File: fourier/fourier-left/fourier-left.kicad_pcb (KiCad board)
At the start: 2 copper layers, 124.4 x 80.4 mm, 129 parts, among them J1 VCC, J3 RGB, J6 C6, J7 GND, U1 ProMicro, U2 TRRS

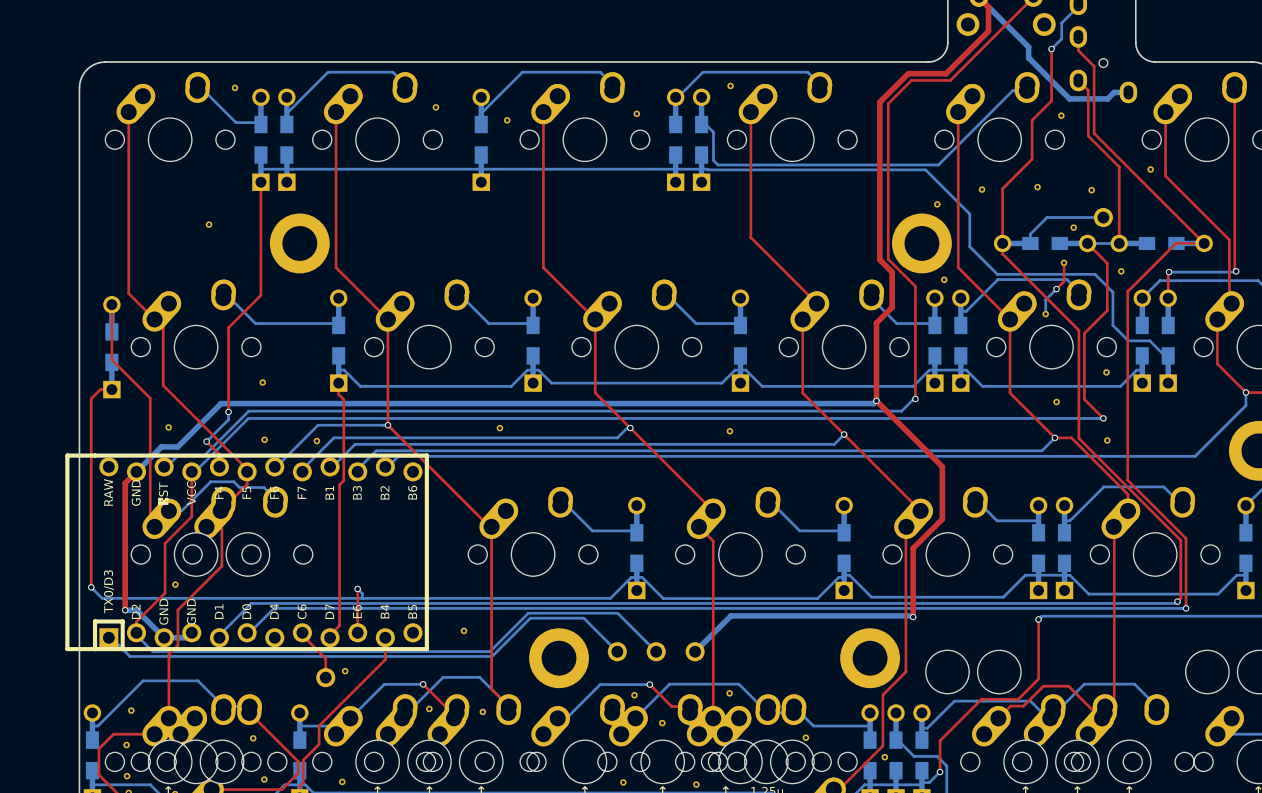
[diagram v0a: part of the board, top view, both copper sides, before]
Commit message: Alas v1
moved pro micro location and added a USB C port for pigtail cables
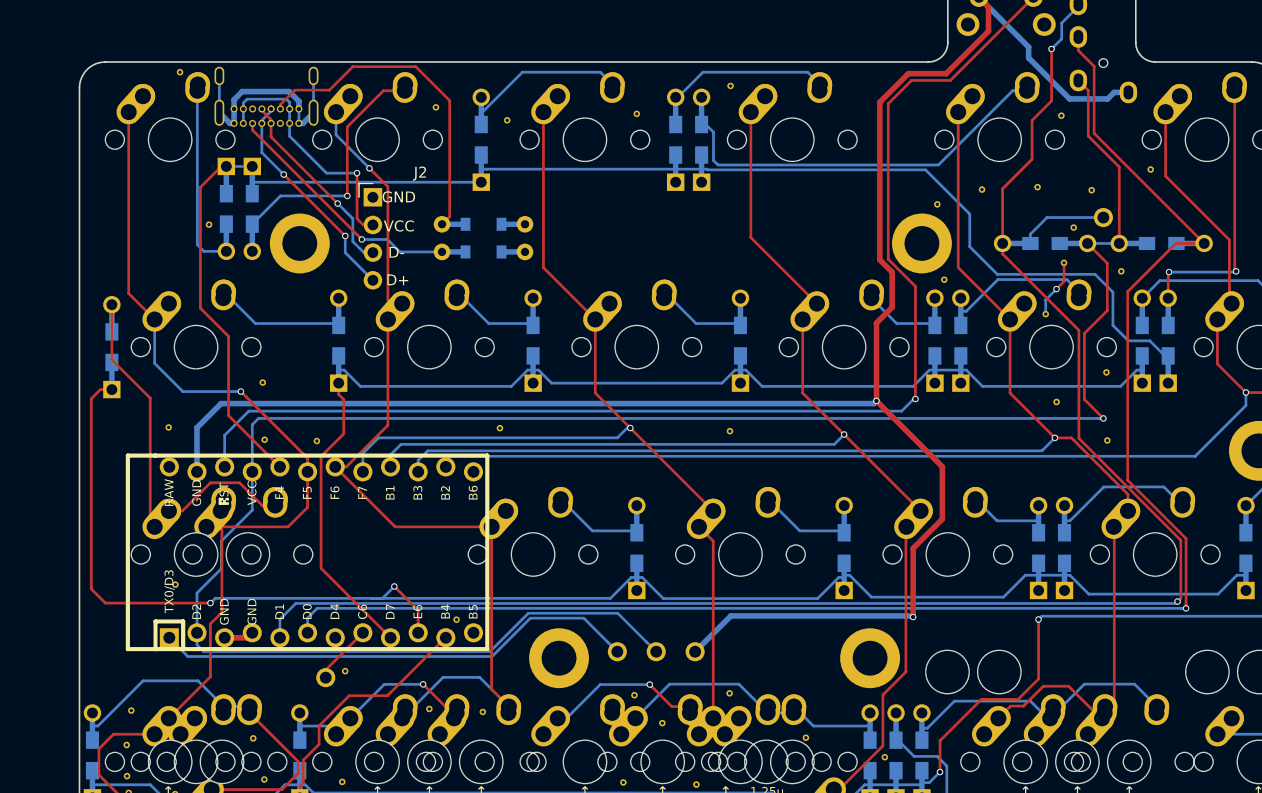
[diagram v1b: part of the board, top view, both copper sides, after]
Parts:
- added J2: Conn_01x04_Female, Connector_PinHeader_2.54mm:PinHeader_1x04_P2.54mm_Horizontal, F.Cu at (43.6, 30.3)
- added J4: USB_C_Receptacle_USB2.0, Type-C:USB_C_GCT_USB4085, B.Cu at (33.8, 17.4)
- added R3: 5.1k, combodiode:ComboResistor, F.Cu at (53.8, 35.3)
- added R4: 5.1k, combodiode:ComboResistor, F.Cu at (53.8, 32.8)
- moved D_A2 7.10 mm to (32.5, 31.4), turned to 90 degrees
- moved D_A1 7.10 mm to (30.2, 31.4), turned to 90 degrees
- moved U1 5.56 mm to (38.9, 62.9)
- moved REF** 5.25 mm to (25.9, 18.8)
- moved REF** 1.24 mm to (51.3, 69.1)
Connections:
- SW_A1 pad 2: Net-(D_A1-Pad2) -> Net-(D1-Pad2)
- SW_A2 pad 2: Net-(D_A2-Pad2) -> Net-(D2-Pad2)
- SW_A3 pad 2: Net-(D_A3-Pad2) -> Net-(D3-Pad2)
- SW_A4 pad 2: Net-(D_A4-Pad2) -> Net-(D4-Pad2)
- SW_A5 pad 2: Net-(D_A5-Pad2) -> Net-(D5-Pad2)
- SW_A6 pad 2: Net-(D_A6-Pad2) -> Net-(D6-Pad2)
- SW_B1 pad 2: Net-(D_B1-Pad2) -> Net-(D7-Pad2)
- SW_B2 pad 2: Net-(D_B2-Pad2) -> Net-(D8-Pad2)
- SW_B3 pad 2: Net-(D_B3-Pad2) -> Net-(D9-Pad2)
- SW_B4 pad 2: Net-(D_B4-Pad2) -> Net-(D10-Pad2)
- SW_B5 pad 2: Net-(D_B5-Pad2) -> Net-(D11-Pad2)
- SW_B6 pad 2: Net-(D_B6-Pad2) -> Net-(D12-Pad2)
- SW_C1 pad 2: Net-(D_C1-Pad2) -> Net-(D13-Pad2)
- SW_C2 pad 2: Net-(D_C2-Pad2) -> Net-(D14-Pad2)
- SW_C3 pad 2: Net-(D_C3-Pad2) -> Net-(D15-Pad2)
- SW_C4 pad 2: Net-(D_C4-Pad2) -> Net-(D16-Pad2)
- SW_C5 pad 2: Net-(D_C5-Pad2) -> Net-(D17-Pad2)
- SW_C6 pad 2: Net-(D_C6-Pad2) -> Net-(D18-Pad2)
- SW_Cb1 pad 1: Net-(D_C1-Pad2) -> Net-(D13-Pad2)
- SW_D1 pad 2: Net-(D_D1-Pad2) -> Net-(D19-Pad2)
- SW_D2 pad 2: Net-(D_D2-Pad2) -> Net-(D20-Pad2)
- SW_D3 pad 1: Net-(D_D3-Pad2) -> Net-(SW_D3-Pad1)
- SW_D4 pad 2: Net-(D_D4-Pad2) -> Net-(D21-Pad2)
- SW_D5 pad 1: Net-(D_D5-Pad2) -> Net-(D22-Pad2)
- SW_D6 pad 2: Net-(D_D6-Pad2) -> Net-(D23-Pad2)
- SW_Db1 pad 2: Net-(D_D1-Pad2) -> Net-(D19-Pad2)
- SW_Db2 pad 1: Net-(D_D2-Pad2) -> Net-(D20-Pad2)
- SW_Db3 pad 2: Net-(D_D3-Pad2) -> Net-(SW_D3-Pad1)
- SW_Db5 pad 2: Net-(D_D5-Pad2) -> Net-(D22-Pad2)
- SW_Dc1 pad 1: Net-(D_D1-Pad2) -> Net-(D19-Pad2)
- SW_Dc2 pad 1: Net-(D_D2-Pad2) -> Net-(D20-Pad2)
- SW_Dc3 pad 2: Net-(D_D3-Pad2) -> Net-(SW_D3-Pad1)
- SW_Dc5 pad 2: Net-(D_D5-Pad2) -> Net-(D22-Pad2)
- SW_Dd3 pad 2: Net-(D_D3-Pad2) -> Net-(SW_D3-Pad1)
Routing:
- net Net-(J4-PadB5): track 0.00 -> 30.3 mm
- net Net-(J2-Pad2): track 0.00 -> 23.0 mm, vias 0 -> 1
- net Net-(J4-PadA5): track 0.00 -> 22.7 mm, vias 0 -> 1
- net Net-(J2-Pad4): track 0.00 -> 20.4 mm, vias 0 -> 2
- net Net-(J2-Pad3): track 0.00 -> 17.9 mm, vias 0 -> 1
- net col1: track 79.1 -> 93.5 mm, vias 0 -> 1
- net Net-(D_A1-Pad2): track 7.25 -> 17.1 mm
- net Net-(D_A2-Pad2): track 13.8 -> 22.8 mm, vias 0 -> 1
- net VCC: track 192.2 -> 184.8 mm
- net RGB: track 50.3 -> 44.6 mm
- net col6: track 155.0 -> 149.6 mm
- net col4: track 117.9 -> 112.9 mm
- net data: track 151.2 -> 146.4 mm
- net col5: track 139.3 -> 134.5 mm
- net data2: track 162.1 -> 157.7 mm
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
